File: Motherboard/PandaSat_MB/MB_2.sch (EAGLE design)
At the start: 92 parts, among them J1 503182-1852, J2 10118194-0001LF, J3 DCJ0303, Q10 IRLML5103, Q11 IRLML5103, Q13 IRLML2803, Q14 IRLML2803, Q15 IRLML2803, Q16 IRLML5103, Q17 2N5088, U1 MAX706R, U2 LTC4121-4.2, U3 LSM9DS1, U4 PE014006, U5 MAX4372TEUK+T, U6 RFM23BP, U7 TPS54226PWPRPWP14_2P31X2P46-L, U8 ATSAMD51, U9 OKL-T3-W12, X1 BU-SMA-V

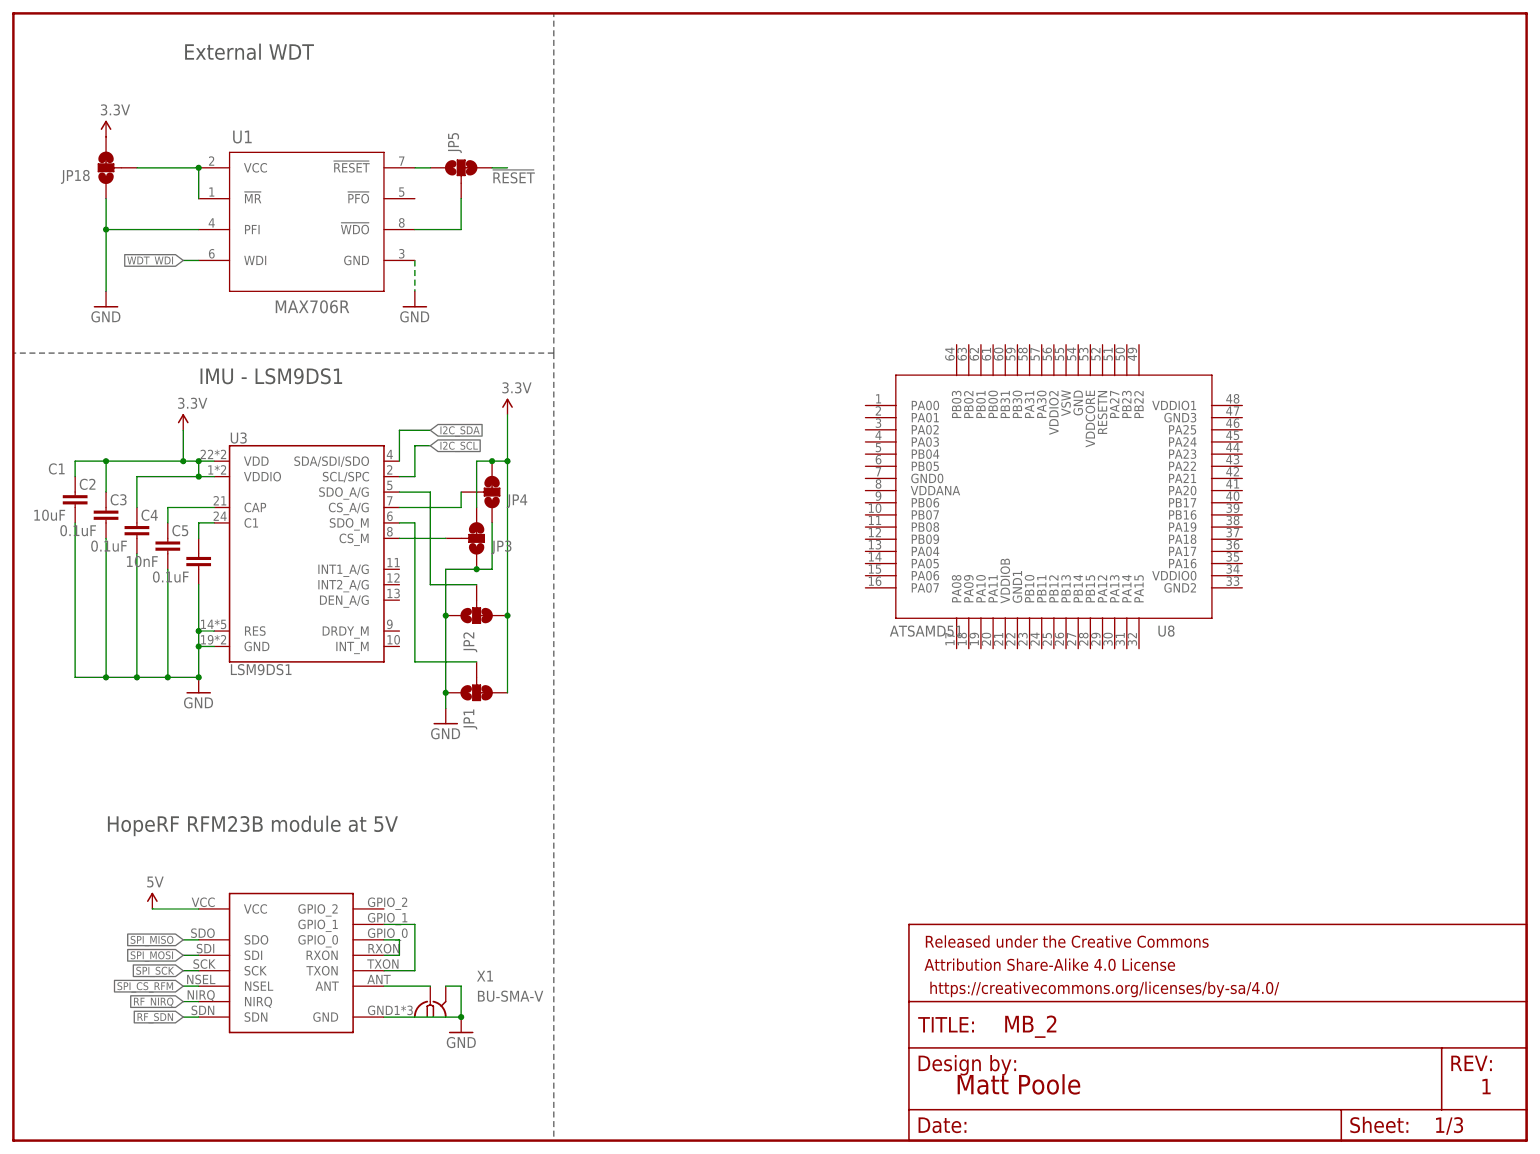
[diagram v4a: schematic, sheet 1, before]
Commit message: More mobo schematic work incl Hbridge, battery and regulator circuitry
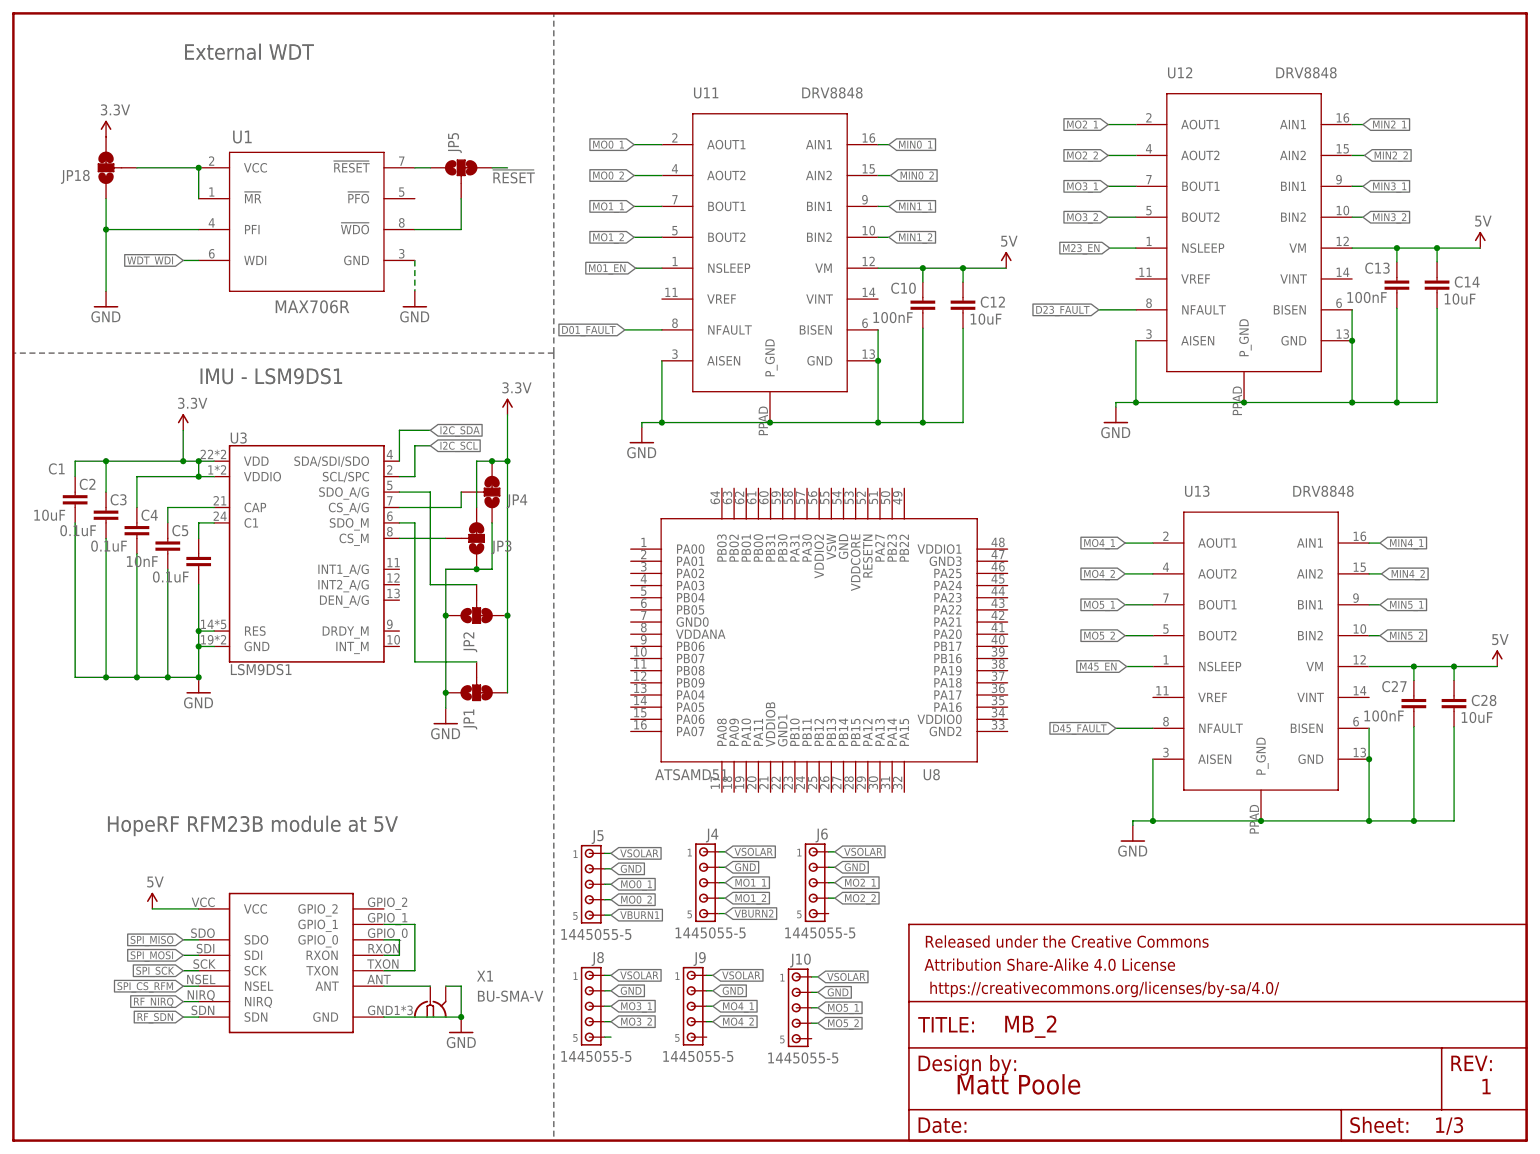
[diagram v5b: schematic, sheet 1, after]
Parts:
- removed JP13, JP16: M023.5MM_LOCK, SparkFun-Connectors:M023.5MM_LOCK
- removed JP19, JP9: (no value), SparkFun-Connectors:M03POLAR_LOCK
- removed JP6: JUMPER-PAD-3-2OF3_NC_BY_TRACE_SMALL, SparkFun-Passives:JUMPER-PAD-3-2OF3_NC_BY_TRACE_SMALL
- added C10, C13: 100nF, SparkFun-Capacitors:10UF-0603-6.3V-20%
- added C11: 2.2uF, SparkFun-Capacitors:2.2UF-0603-10V-20%
- added C12, C14, C28, C6, C7, C8, C9: 10uF, SparkFun-Capacitors:10UF-0603-6.3V-20%
- added D3, D6: DFLS130L, BrownSpaceEngineering:DFLS130L
- added J10, J4, J5, J6, J8, J9: 1445055-5, con-amp:1445055-5
- added J7: BK-18650, pandasat:BK-18650
- added L1: 3.3uH, BrownSpaceEngineering:IND1812
- added Q1: (no value), transistor-power:N-MOSFET-SO8S
- added R23: 1.34K, resistor:R-US_R0603
- added U11, U12, U13: DRV8848, pandasat:DRV8848
- C27: value 2.2uF -> 100nF; device SparkFun-Capacitors:2.2UF-0603-10V-20% -> SparkFun-Capacitors:10UF-0603-6.3V-20%
- R21: value 1K34 -> 100k
- R22: value 100K -> 100k
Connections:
- removed net N$43: J3.2, J3.3, JP10.2, JP11.2, JP12.1
- new net 5V2: C11.1, D3.A, F2.2
- new net 5V_EN: Q1.G
- new net D01_FAULT: U11.NFAULT
- new net D23_FAULT: U12.NFAULT
- new net D45_FAULT: U13.NFAULT
- new net M01_EN: U11.NSLEEP
- new net M23_EN: U12.NSLEEP
- new net M45_EN: U13.NSLEEP
- new net MIN0_1: U11.AIN1
- new net MIN0_2: U11.AIN2
- new net MIN1_1: U11.BIN1
- new net MIN1_2: U11.BIN2
- new net MIN2_1: U12.AIN1
- new net MIN2_2: U12.AIN2
- new net MIN3_1: U12.BIN1
- new net MIN3_2: U12.BIN2
- new net MIN4_1: U13.AIN1
- new net MIN4_2: U13.AIN2
- new net MIN5_1: U13.BIN1
- new net MIN5_2: U13.BIN2
- new net MO0_1: J5.3, U11.AOUT1
- new net MO0_2: J5.4, U11.AOUT2
- new net MO1_1: J4.3, U11.BOUT1
- new net MO1_2: J4.4, U11.BOUT2
- new net MO2_1: J6.3, U12.AOUT1
- new net MO2_2: J6.4, U12.AOUT2
- new net MO3_1: J8.3, U12.BOUT1
- new net MO3_2: J8.4, U12.BOUT2
- new net MO4_1: J9.3, U13.AOUT1
- new net MO4_2: J9.4, U13.AOUT2
- new net MO5_1: J10.3, U13.BOUT1
- new net MO5_2: J10.4, U13.BOUT2
- new net N$27: J8.5
- new net N$29: D6.A, J7.1N, J7.2N, J7.3N, J7.4N, JP12.1
- new net N$30: D6.C, J3.2, J3.3
- new net VBATT_IN: D3.C, J7.1P, J7.2P, J7.3P, J7.4P, JP10.2
- net 3.3V: no longer Q16.S, R20.1
- net 5V: now also C10.1, C12.1, C13.1, C14.1, C28.1, C8.1, C9.1, L1.P$1, Q16.S, R20.1, U11.VM, U12.VM, U13.VM; no longer F2.2, JP10.1, JP11.1, JP13.2, U9.VOUT1
- net GND: now also C10.2, C11.2, C12.2, C13.2, C14.2, C28.2, C6.2, C7.2, C8.2, C9.2, J10.2, J4.2, J5.2, J6.2, J8.2, J9.2, R21.1, R23.2, U11.AISEN, U11.BISEN, U11.GND, U11.P_GND, U12.AISEN, U12.BISEN, U12.GND, U12.P_GND, U13.AISEN, U13.BISEN, U13.GND, U13.P_GND; no longer JP19.1, JP9.1, R21.2
- net N$18: now also Q1.S, R21.2, U9.ON/OFF; no longer R21.1, U9.TRIM1
- net N$19: now also R23.1, U9.TRIM; no longer JP6.1, U9.ON/OFF
- net N$22: now also L1.P$2, U9.VOUT1; no longer JP6.2, U9.VIN
- net N$4: now also JP10.1, JP11.2; no longer JP13.1, JP16.2
- net VBATT: now also JP11.1, Q1.D; no longer JP16.1, JP6.3
- net VBURN1: now also J5.5; no longer JP9.3
- net VBURN2: now also J4.5; no longer JP19.3
- net VREG_IN: now also C6.1, C7.1, U9.VIN
- net VSOLAR: now also J10.1, J4.1, J5.1, J6.1, J8.1, J9.1; no longer JP19.2, JP9.2
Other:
- note added: "Regulator - 5V OUT"
- moved on the sheet: F2, J2, J3, JP10, JP11, JP12, R21, R22, U8, U9

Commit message: Rearranged schematics and added payload connection
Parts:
- added FRAME4: FRAME-LETTER, SparkFun-Aesthetics:FRAME-LETTER
- added JP6: (no value), SparkFun-Connectors:M04JST-PTH-VERT
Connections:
- new net PL_UART_RX: JP6.1
- new net PL_UART_TX: JP6.2
- net GND: now also JP6.3
- net PL_PWR_IN: now also JP6.4
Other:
- note added: "H-Bridges"
- note added: "Payload Connector"
- note added: "Solar Panel Connectors"
- note removed: "Antenna Board Connectors"

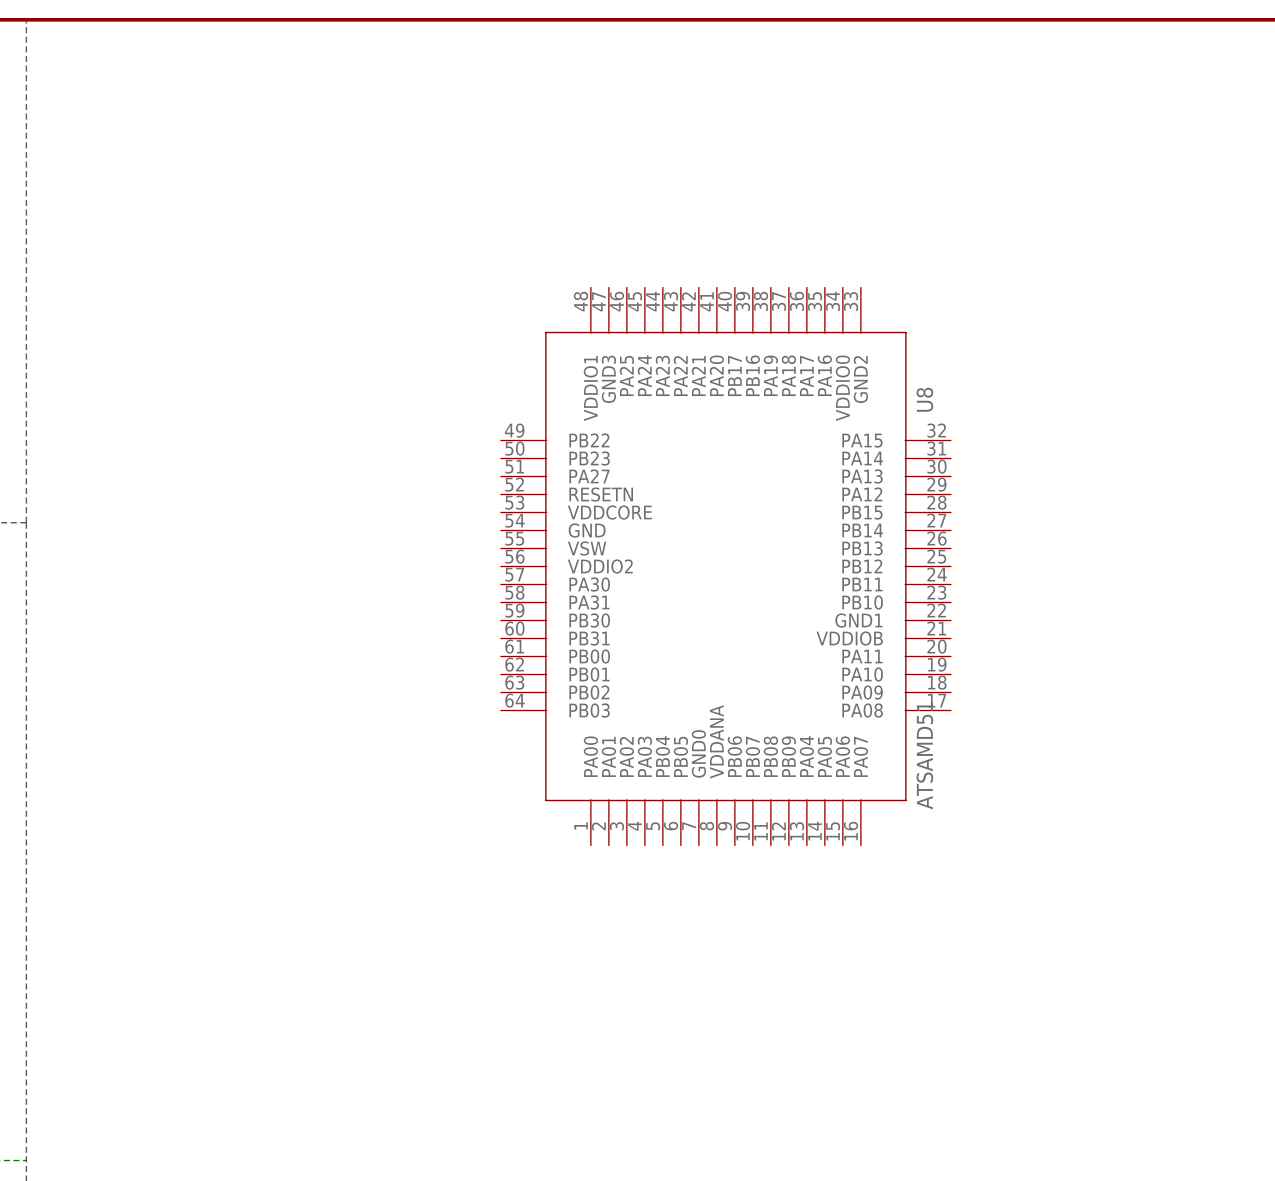
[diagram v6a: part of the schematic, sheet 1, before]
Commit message: Updated Samd51 symbol, Changed Battery config to 2s2p, Added Power + Osc to MCU
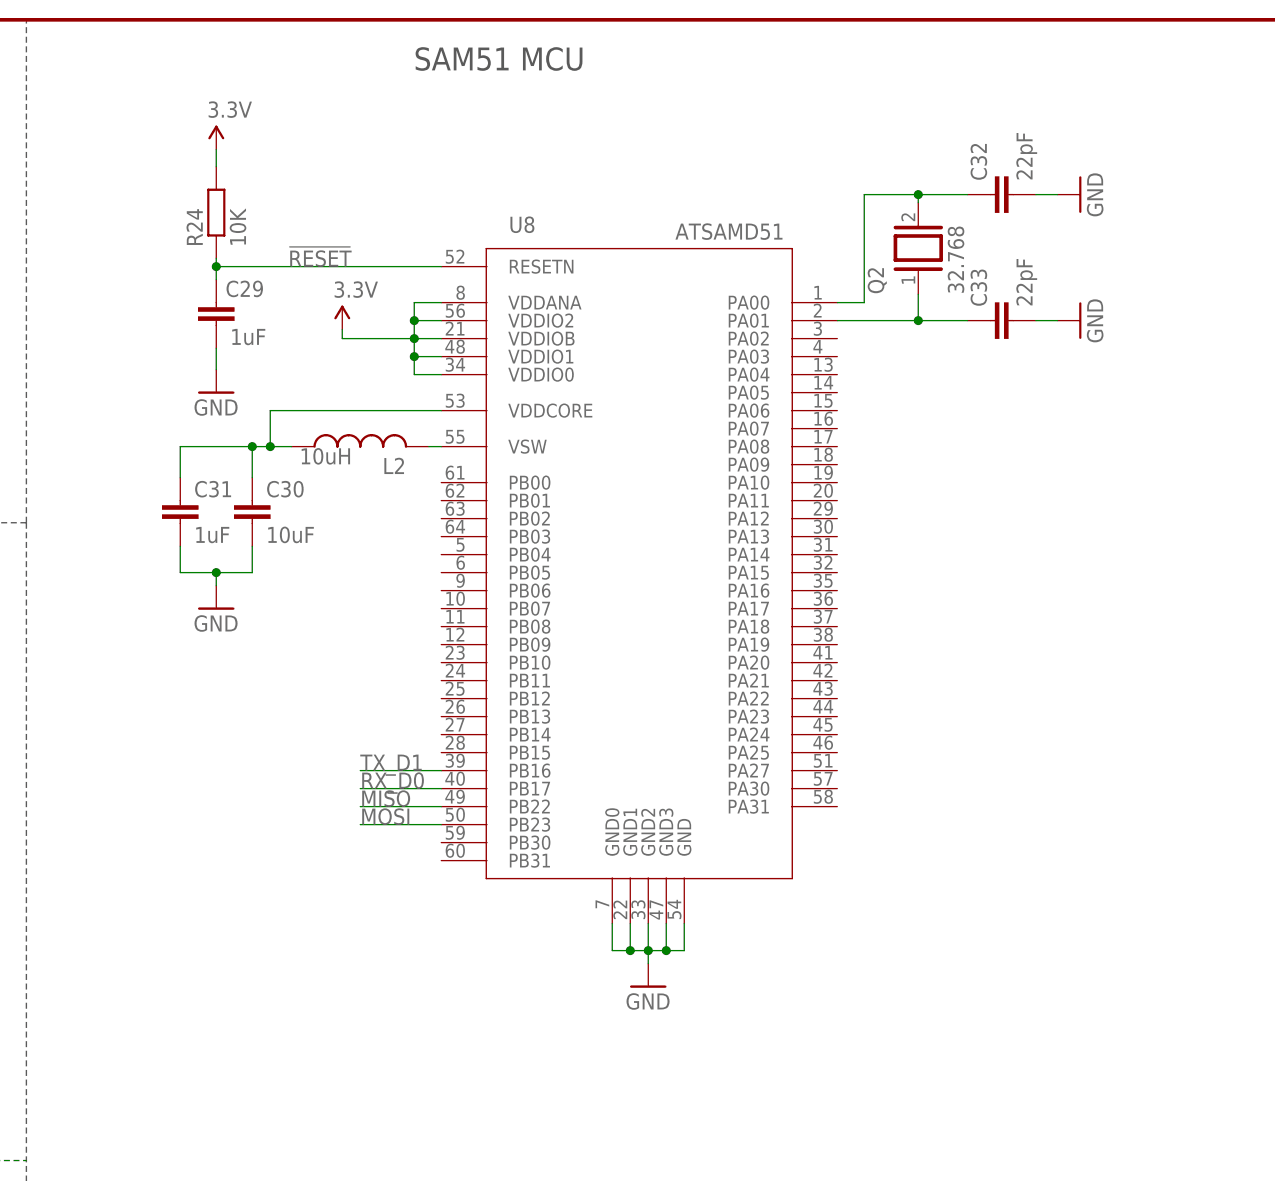
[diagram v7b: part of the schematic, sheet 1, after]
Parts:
- added C29, C31: 1uF, resistor:C-EUC0805
- added C30: 10uF, resistor:C-EUC0805
- added C32, C33: 22pF, resistor:C-EUC0603
- added L2: 10uH, resistor:L-USL4532C
- added Q2: 32.768, special:XTAL
- added R24: 10K, resistor:R-EU_R0603
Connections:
- new net MISO: U8.PB22
- new net MOSI: U8.PB23
- new net N$40: D6.A, J7.1N, J7.2N, JP12.1
- new net N$41: J7.1P, J7.2P, J7.3N, J7.4N
- new net N$42: L2.2, U8.VSW
- new net N$43: C30.1, C31.1, L2.1, U8.VDDCORE
- new net N$44: C33.1, Q2.1, U8.PA01
- new net RX_D0: U8.PB17
- new net TX_D1: U8.PB16
- net !RESET: now also C29.1, R24.1, U8.RESETN
- net 3.3V: now also R24.2, U8.VDDANA, U8.VDDIO0, U8.VDDIO1, U8.VDDIO2, U8.VDDIOB
- net GND: now also C29.2, C30.2, C31.2, C32.2, C33.2, U8.GND, U8.GND0, U8.GND1, U8.GND2, U8.GND3
- net N$29: now also C32.1, Q2.2, U8.PA00; no longer D6.A, J7.1N, J7.2N, J7.3N, J7.4N, JP12.1
- net VBATT_IN: no longer J7.1P, J7.2P
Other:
- note added: "Batterys in 2s2p config"
- note added: "SAM51 MCU"
- moved on the sheet: U8
